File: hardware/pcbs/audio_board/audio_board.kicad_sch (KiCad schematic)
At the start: 18 parts, among them J1 I2C, J2 MTA100_08, J3 NC3MAH, J4 AudioJack3, J5 NC3MAH

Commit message: component values
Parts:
- J1: MPN (none) -> Header_1x04; Part Header_1x04 -> (none)
- J2: MPN (none) -> 640457-8; Part 640457-8 -> (none); Shop https://eu.mouser.com/ProductDetail/TE-Connectivity/640457-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 -> (none)
- J4: Part SJ1-3533NG -> (none); Shop https://eu.mouser.com/ProductDetail/490-SJ1-3533NG -> (none)
- R1, R2, R3, R4: LCSC C21190 -> (none); Part R 1kΩ 125mW 1% 0603 -> (none); Shop https://store.comet.bg/Catalogue/Product/4405/ -> (none)
- R5, R6, R7: LCSC C23182 -> (none); MPN 560112116054 -> (none); Part R 47Ω 125mW 1% 0603 -> (none); Shop https://store.comet.bg/Catalogue/Product/4392/ -> (none)
- R8: LCSC C23182 -> (none); MPN 560112116054 -> R 0Ω 125mW 1% 0805; Part R 47Ω 125mW 1% 0603 -> (none); Shop https://store.comet.bg/Catalogue/Product/4392/ -> (none)
- U1: Part 2x HeaderSocket_1x24, Teensy 4.1 -> (none); Shop https://store.comet.bg/Catalogue/Product/10086/ -> (none)

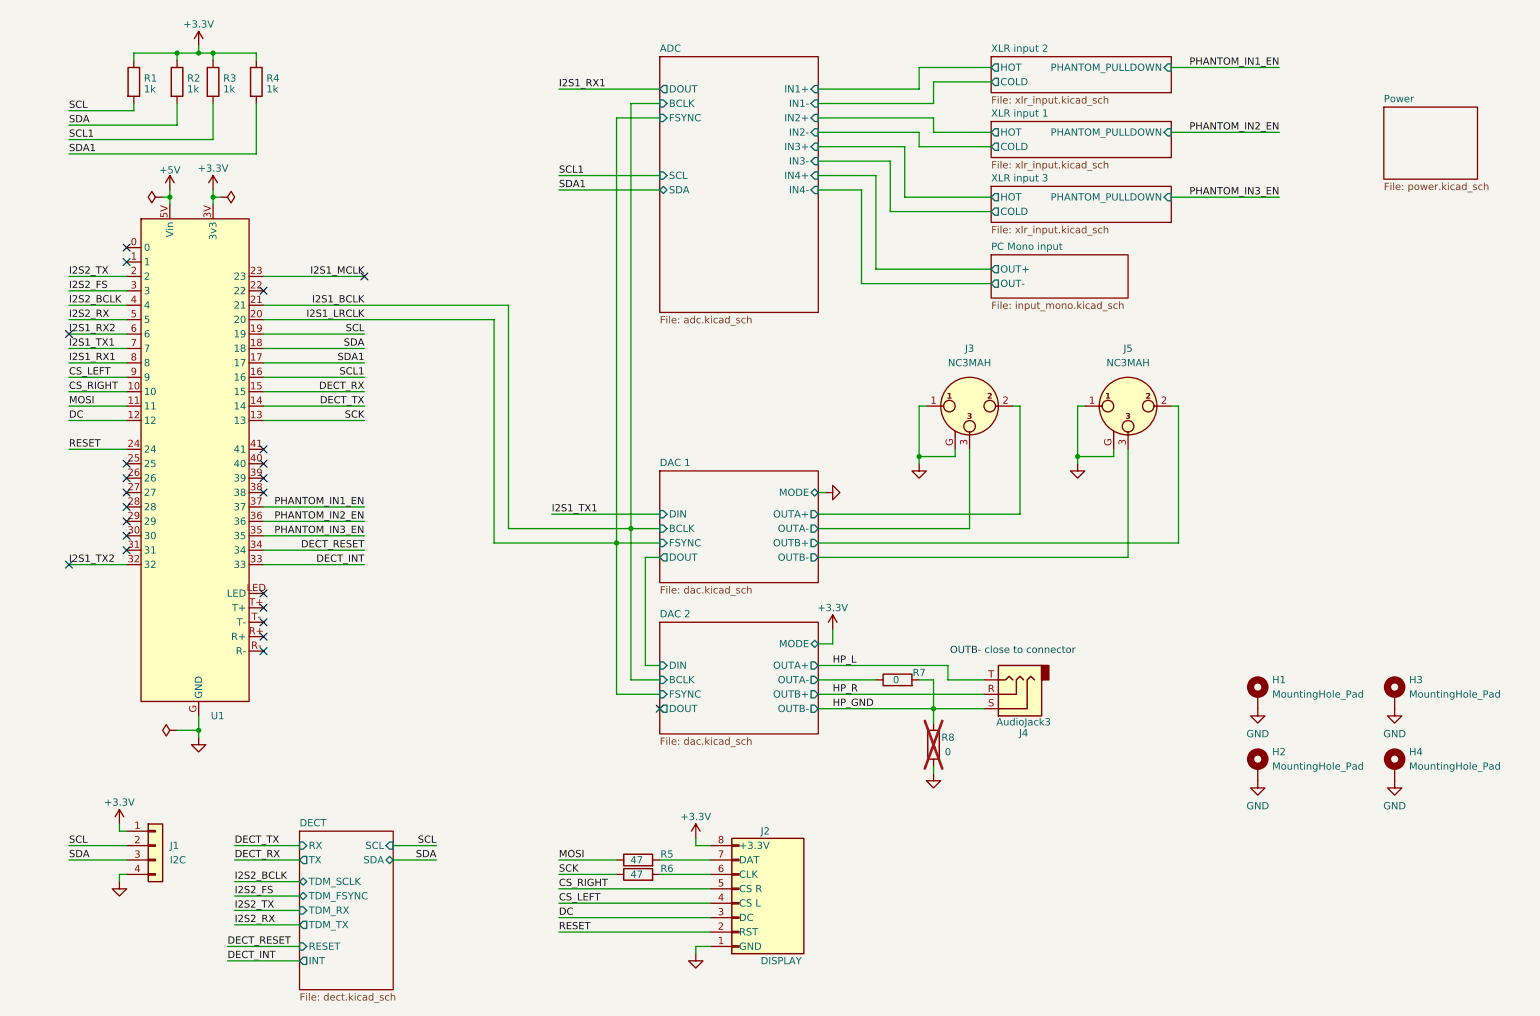
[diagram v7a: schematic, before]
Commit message: revise BOM
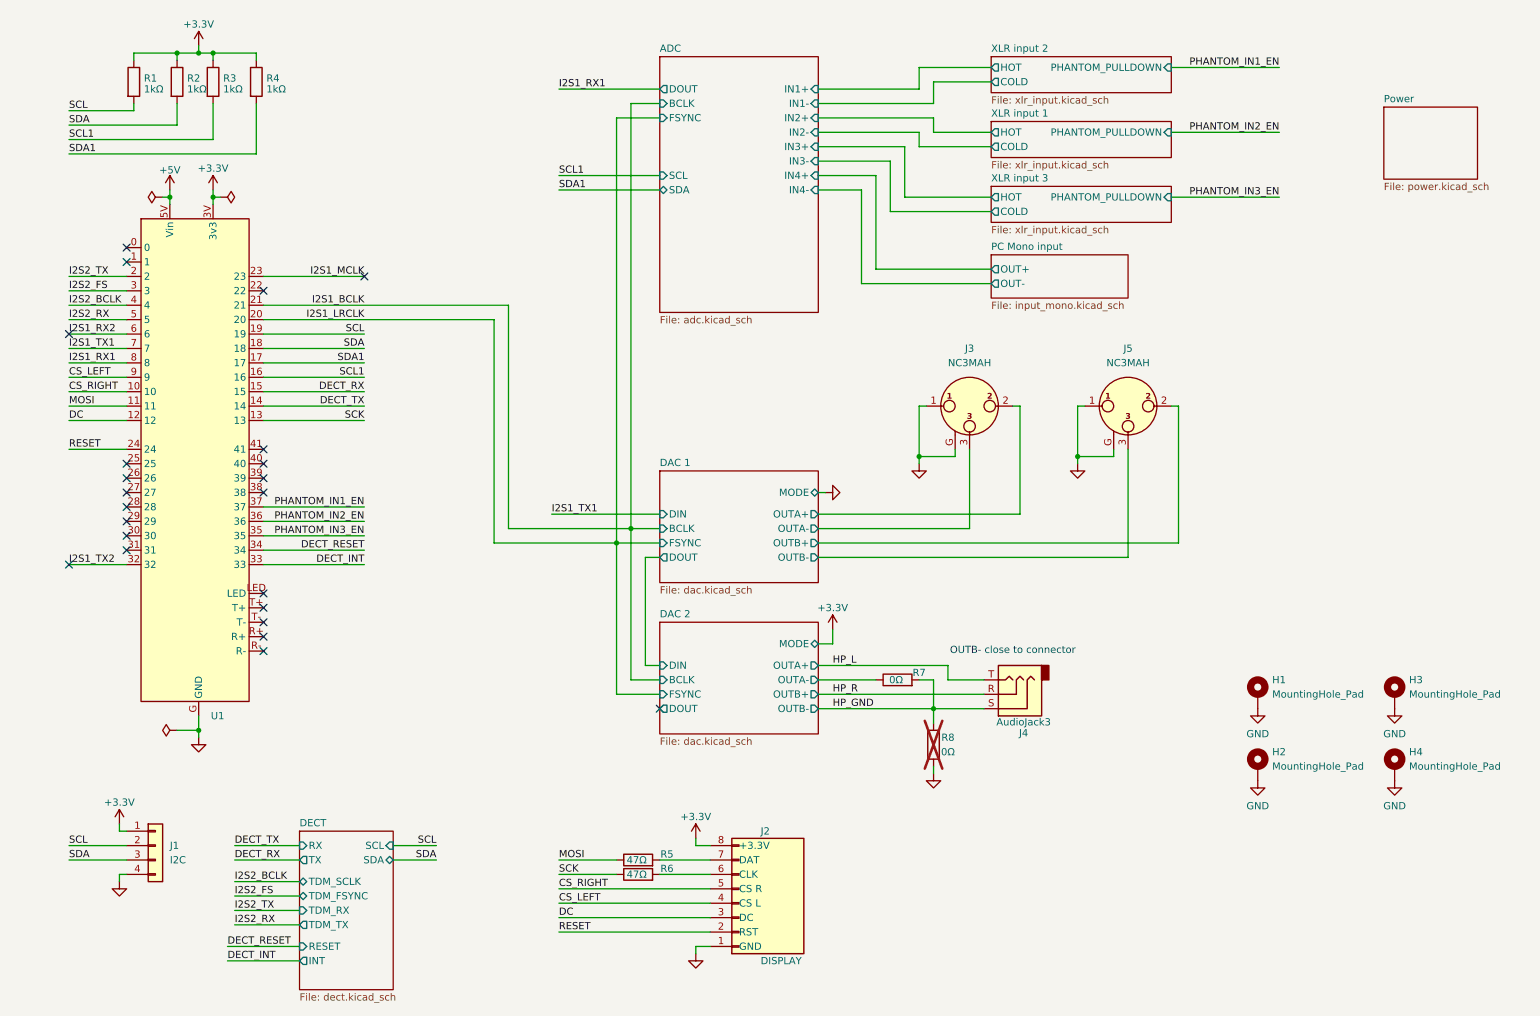
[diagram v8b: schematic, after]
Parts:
- J1: MPN Header_1x04 -> PinHeader_1x04
- J4: Purpose (none) -> Internal mono in
- R1, R2, R3, R4: value 1k -> 1kΩ; MPN (none) -> R 1kΩ 125mW 1% 0805
- R5, R6: value 47 -> 47Ω; MPN (none) -> R 47Ω 125mW 1% 0805
- R7: value 0 -> 0Ω; MPN (none) -> R 0Ω 125mW 1% 0805
- R8: value 0 -> 0Ω
- U1: value ~ -> Teensy 4.1; MPN (none) -> 2x PinSocket_1x24
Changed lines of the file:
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@@
 			)
 		)
-		(property "Value" "1k"
+		(property "Value" "1kΩ"
 			(at 46.228 29.2173 0)
 			(effects
@@
 		)
 		(property "Description" ""
+			(at 44.45 27.94 0)
+			(effects
+				(font
+					(size 1.27 1.27)
+				)
+				(hide yes)
+			)
+		)
+		(property "MPN" "R 1kΩ 125mW 1% 0805"
 			(at 44.45 27.94 0)
 			(effects
@@
 			)
 		)
-		(property "Value" "1k"
+		(property "Value" "1kΩ"
 			(at 38.608 29.2173 0)
 			(effects
@@
 			)
 		)
+		(property "MPN" "R 1kΩ 125mW 1% 0805"
+			(at 36.83 27.94 0)
+			(effects
+				(font
+					(size 1.27 1.27)
+				)
+				(hide yes)
+			)
+		)
 		(pin "1"
 		)
@@
 			)
 		)
-		(property "Value" "47"
+		(property "Value" "47Ω"
 			(at 125.476 165.1 90)
 			(effects
@@
 			)
 		)
-		(property "MPN" ""
+		(property "MPN" "R 47Ω 125mW 1% 0805"
 			(at 125.73 165.1 0)
 			(effects
@@
 			)
 		)
-		(property "Value" "1k"
+		(property "Value" "1kΩ"
 			(at 60.198 29.2173 0)
 			(effects
@@
 		)
 		(property "Description" ""
+			(at 58.42 27.94 0)
+			(effects
+				(font
+					(size 1.27 1.27)
+				)
+				(hide yes)
+			)
+		)
+		(property "MPN" "R 1kΩ 125mW 1% 0805"
 			(at 58.42 27.94 0)
 			(effects
@@
 			)
 		)
+		(property "Purpose" "Internal mono in"
+			(at 191.77 135.89 0)
+			(effects
+				(font
+					(size 1.27 1.27)
+				)
+				(hide yes)
+			)
+		)
 		(pin "R"
 		)
@@
 			)
 		)
-		(property "Value" "47"
+		(property "Value" "47Ω"
 			(at 125.476 167.64 90)
 			(effects
@@
 			)
 		)
-		(property "MPN" ""
+		(property "MPN" "R 47Ω 125mW 1% 0805"
 			(at 125.73 167.64 0)
 			(effects
@@
 			)
 		)
-		(property "Value" "0"
+		(property "Value" "0Ω"
 			(at 171.196 133.35 90)
 			(effects
@@
 			)
 		)
-		(property "MPN" ""
+		(property "MPN" "R 0Ω 125mW 1% 0805"
 			(at 171.45 133.35 0)
 			(effects
@@
 			)
 		)
-		(property "MPN" "Header_1x04"
+		(property "MPN" "PinHeader_1x04"
 			(at 40.64 162.56 0)
 			(effects
@@
 			)
 		)
-		(property "Value" "1k"
+		(property "Value" "1kΩ"
 			(at 52.578 29.2173 0)
 			(effects
@@
 		)
 		(property "Description" ""
+			(at 50.8 27.94 0)
+			(effects
+				(font
+					(size 1.27 1.27)
+				)
+				(hide yes)
+			)
+		)
+		(property "MPN" "R 1kΩ 125mW 1% 0805"
 			(at 50.8 27.94 0)
 			(effects
@@
 			)
 		)
-		(property "Value" "~"
+		(property "Value" "Teensy 4.1"
 			(at 50.4033 142.24 0)
 			(effects
@@
 		)
 		(property "Description" ""
+			(at 48.26 50.8 0)
+			(effects
+				(font
+					(size 1.27 1.27)
+				)
+				(hide yes)
+			)
+		)
+		(property "MPN" "2x PinSocket_1x24"
 			(at 48.26 50.8 0)
 			(effects
@@
 			)
 		)
-		(property "Value" "0"
+		(property "Value" "0Ω"
 			(at 180.34 146.05 0)
 			(effects
